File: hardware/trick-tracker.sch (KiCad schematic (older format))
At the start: 52 parts, among them IC1 BMX160, J1 USB4105-GF-A, J2 S2B-PH-K, J3 QWiiC, J4 MEM2061-01-188-00-A, J6 QWiiC, P1 SMTB-1240-S-R, U1 MS88SF2, U2 DPS368XTSA1, U4 MCP73831/OT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

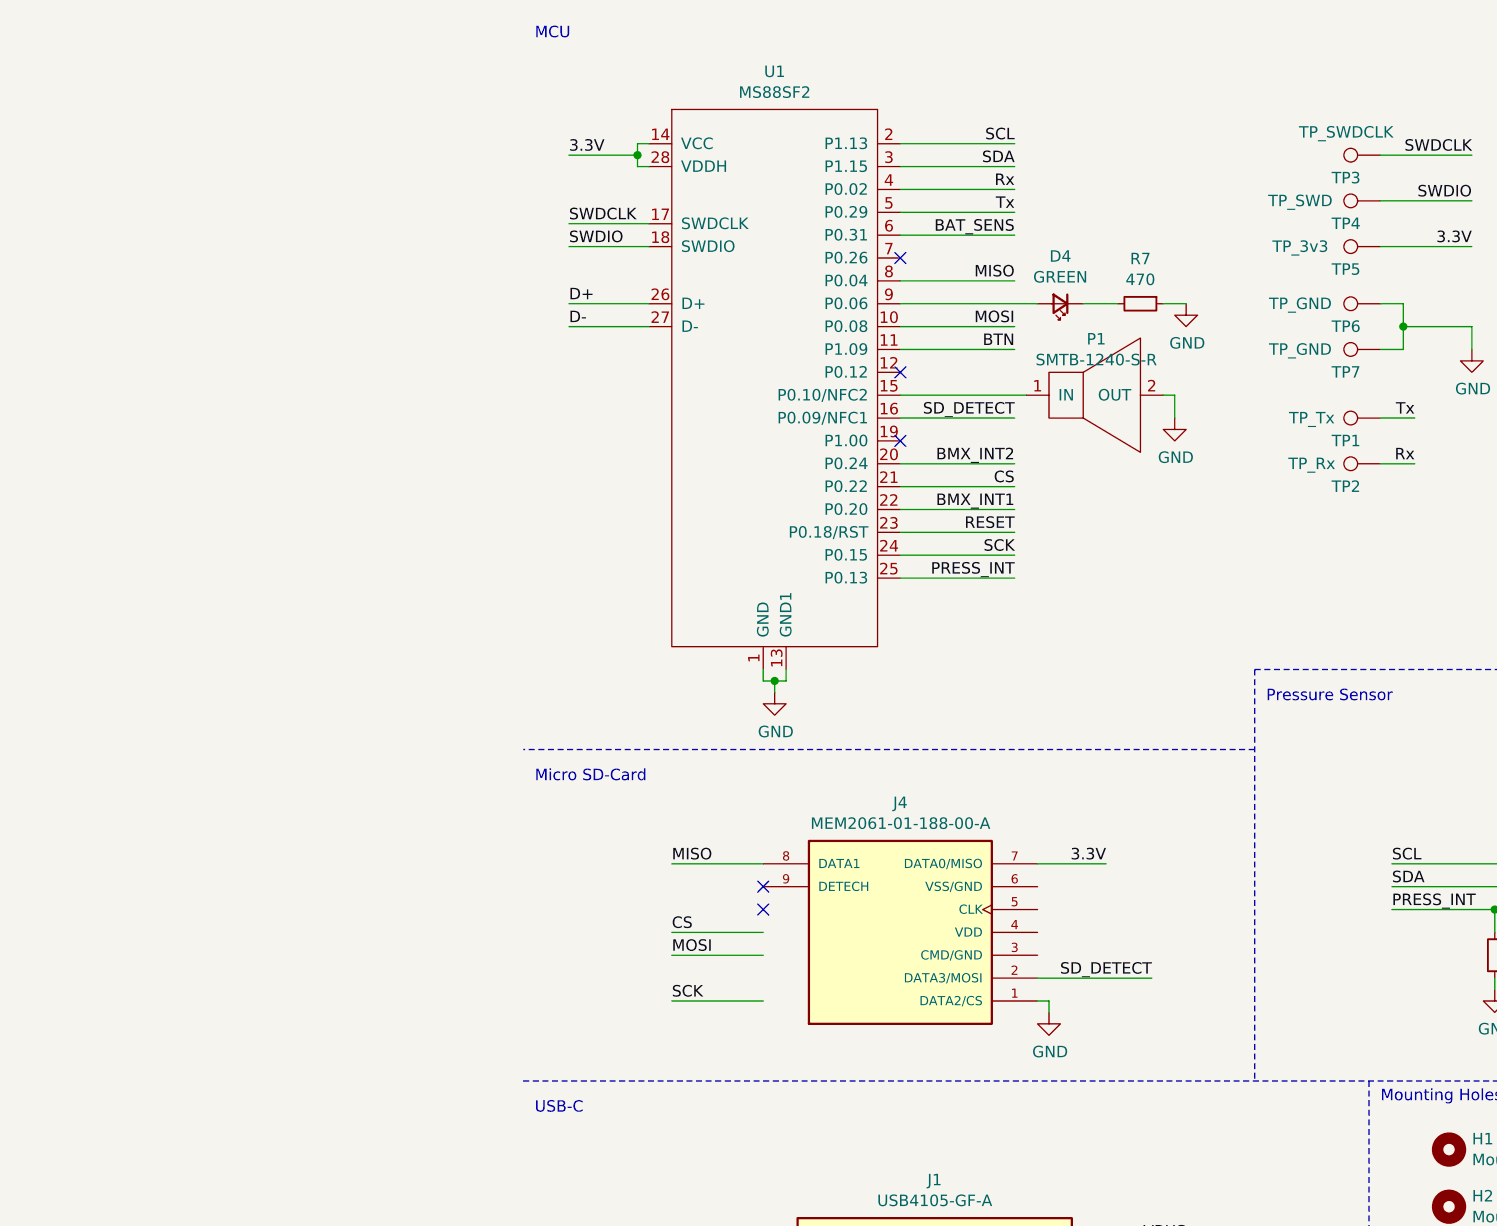
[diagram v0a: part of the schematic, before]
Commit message: Changed Layout to use ESP32 instead of nRF52
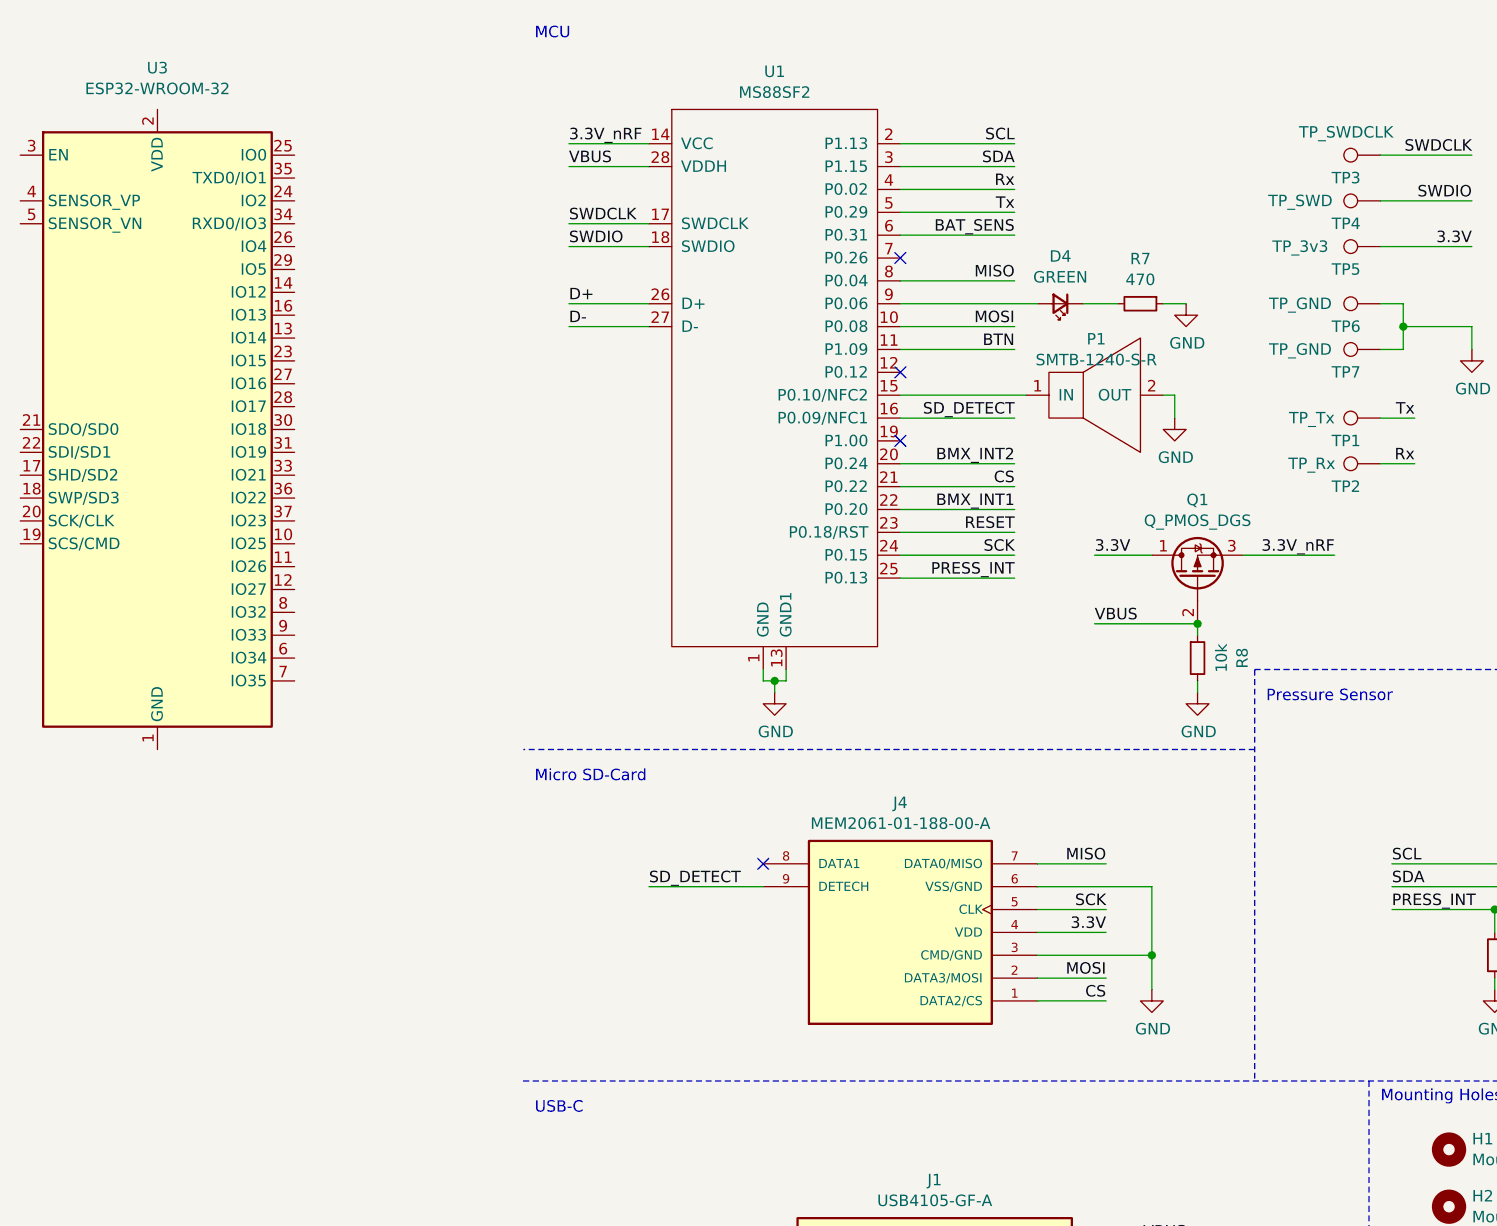
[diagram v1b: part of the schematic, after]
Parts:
- added Q1: Q_PMOS_DGS, symbol Device:Q_PMOS_DGS
- added R8: 10k, Resistor_SMD:R_0603_1608Metric, symbol Device:R_Small
- added U3: ESP32-WROOM-32, RF_Module:ESP32-WROOM-32, symbol RF_Module:ESP32-WROOM-32
- J4: footprint MEM2061-01-188-00-A_REVA:GCT_MEM2061-01-188-00-A_REVA -> GCT_MEM2051-00-195-00-A; MANUFACTURER (none) -> GCT
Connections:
- net 3.3V: now also J4.4 (VDD), Q1.1 (D); no longer J4.7 (DATA0/MISO), U1.14 (VCC), U1.28 (VDDH)
- net CS: now also J4.1 (DATA2/CS)
- net GND: now also J4.3 (CMD/GND), J4.6 (VSS/GND), R8.2; no longer J4.1 (DATA2/CS)
- net MISO: now also J4.7 (DATA0/MISO); no longer J4.8 (DATA1)
- net MOSI: now also J4.2 (DATA3/MOSI)
- net SCK: now also J4.5 (CLK)
- net SD_DETECT: now also J4.9 (DETECH); no longer J4.2 (DATA3/MOSI)
- net VBUS: now also U1.28 (VDDH), Q1.2 (G), R8.1
- new net: U3.1 (GND), U3.15 (GND), U3.38 (GND), U3.39 (GND)
- new net 3.3V_nRF: Q1.3 (S), U1.14 (VCC)
- no-connect marks 12 -> 11
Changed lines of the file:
@@
 Wire Wire Line
 	1600 3400 1550 3400
-Text Label 700  1100 0    50   ~ 0
-3.3V
-Wire Wire Line
-	1050 1150 1000 1150
-Wire Wire Line
-	1050 1050 1000 1050
-Wire Wire Line
-	1000 1050 1000 1100
-Wire Wire Line
-	700  1100 1000 1100
-Connection ~ 1000 1100
-Wire Wire Line
-	1000 1100 1000 1150
 $Comp
 L Device:D_Schottky D1
@@
 F 0 "J4" H 2150 5067 50  0000 C CNN
 F 1 "MEM2061-01-188-00-A" H 2150 4976 50  0000 C CNN
-F 2 "MEM2061-01-188-00-A_REVA:GCT_MEM2061-01-188-00-A_REVA" H 2150 4500 50  0001 L BNN
+F 2 "GCT_MEM2051-00-195-00-A" H 2150 4500 50  0001 L BNN
 F 3 "" H 2150 4500 50  0001 L BNN
+F 4 "GCT" H 2150 4500 50  0001 C CNN "MANUFACTURER"
 	1    2150 4500
 	1    0    0    -1
@@
 	1    0    0    -1
 $EndComp
+Text Label 3050 4500 2    50   ~ 0
+3.3V
 Text Label 3050 4200 2    50   ~ 0
-3.3V
-Wire Wire Line
-	3050 4200 2750 4200
-Text Label 1150 4200 0    50   ~ 0
 MISO
-Text Label 1150 4600 0    50   ~ 0
+Text Label 3050 4700 2    50   ~ 0
 MOSI
-Text Label 1150 4800 0    50   ~ 0
+Text Label 3050 4400 2    50   ~ 0
 SCK
-NoConn ~ 1550 4300
-NoConn ~ 1550 4400
-Text Label 1150 4500 0    50   ~ 0
+Text Label 3050 4800 2    50   ~ 0
 CS
 $Comp
 L power:GND #PWR0130
 U 1 1 60AF2CE9
-P 2800 4850
-F 0 "#PWR0130" H 2800 4600 50  0001 C CNN
-F 1 "GND" H 2805 4677 50  0000 C CNN
-F 2 "" H 2800 4850 50  0001 C CNN
-F 3 "" H 2800 4850 50  0001 C CNN
-	1    2800 4850
-	1    0    0    -1
-$EndComp
-Wire Wire Line
-	2800 4850 2800 4800
-Wire Wire Line
-	2800 4800 2750 4800
-Wire Wire Line
-	1550 4800 1150 4800
-Wire Wire Line
-	1150 4600 1550 4600
-Wire Wire Line
-	1550 4500 1150 4500
-Wire Wire Line
-	1150 4200 1550 4200
+P 3250 4750
+F 0 "#PWR0130" H 3250 4500 50  0001 C CNN
+F 1 "GND" H 3255 4577 50  0000 C CNN
+F 2 "" H 3250 4750 50  0001 C CNN
+F 3 "" H 3250 4750 50  0001 C CNN
+	1    3250 4750
+	1    0    0    -1
+$EndComp
 $Comp
 L Device:R_Small R7
@@
 Wire Wire Line
 	2650 2850 2150 2850
-Text Label 3250 4700 2    50   ~ 0
+Text Label 1050 4300 0    50   ~ 0
 SD_DETECT
-Wire Wire Line
-	3250 4700 2750 4700
 Text Label 2650 2250 2    50   ~ 0
 SD_DETECT
@@
 Wire Wire Line
 	4350 1850 4350 1950
+Wire Wire Line
+	700  1050 1050 1050
+$Comp
+L Device:Q_PMOS_DGS Q1
+U 1 1 6166D587
+P 3450 2950
+F 0 "Q1" V 3792 2950 50  0000 C CNN
+F 1 "Q_PMOS_DGS" V 3701 2950 50  0000 C CNN
+F 2 "" H 3650 3050 50  0001 C CNN
+F 3 "~" H 3450 2950 50  0001 C CNN
+	1    3450 2950
+	0    -1   -1   0
+$EndComp
+Text Label 3000 2850 0    50   ~ 0
+3.3V
+Wire Wire Line
+	3000 2850 3250 2850
+Text Label 4050 2850 2    50   ~ 0
+3.3V_nRF
+Wire Wire Line
+	4050 2850 3650 2850
+Text Label 3000 3150 0    50   ~ 0
+VBUS
+Text Label 700  1150 0    50   ~ 0
+VBUS
+Wire Wire Line
+	1050 1150 700  1150
+Wire Wire Line
+	3000 3150 3450 3150
+$Comp
+L Device:R_Small R8
+U 1 1 616A1F0D
+P 3450 3300
+F 0 "R8" V 3646 3300 50  0000 C CNN
+F 1 "10k" V 3555 3300 50  0000 C CNN
+F 2 "Resistor_SMD:R_0603_1608Metric" H 3450 3300 50  0001 C CNN
+F 3 "~" H 3450 3300 50  0001 C CNN
+	1    3450 3300
+	1    0    0    -1
+$EndComp
+$Comp
+L power:GND #PWR0121
+U 1 1 616A2F85
+P 3450 3450
+F 0 "#PWR0121" H 3450 3200 50  0001 C CNN
+F 1 "GND" H 3455 3277 50  0000 C CNN
+F 2 "" H 3450 3450 50  0001 C CNN
+F 3 "" H 3450 3450 50  0001 C CNN
+	1    3450 3450
+	1    0    0    -1
+$EndComp
+Wire Wire Line
+	3450 3150 3450 3200
+Connection ~ 3450 3150
+Wire Wire Line
+	3450 3400 3450 3450
+Text Label 700  1050 0    50   ~ 0
+3.3V_nRF
+$Comp
+L RF_Module:ESP32-WROOM-32 U3
+U 1 1 61E158C8
+P -1100 2300
+F 0 "U3" H -1100 3881 50  0000 C CNN
+F 1 "ESP32-WROOM-32" H -1100 3790 50  0000 C CNN
+F 2 "RF_Module:ESP32-WROOM-32" H -1100 800 50  0001 C CNN
+F 3 "https://www.espressif.com/sites/default/files/documentation/esp32-wroom-32_datasheet_en.pdf" H -1400 2350 50  0001 C CNN
+	1    -1100 2300
+	1    0    0    -1
+$EndComp
+Wire Wire Line
+	3050 4800 2750 4800
+Wire Wire Line
+	3050 4700 2750 4700
+Wire Wire Line
+	3050 4500 2750 4500
+Wire Wire Line
+	2750 4400 3050 4400
+Wire Wire Line
+	3050 4200 2750 4200
+Wire Wire Line
+	2750 4300 3250 4300
+Wire Wire Line
+	3250 4300 3250 4600
+Wire Wire Line
+	2750 4600 3250 4600
+Connection ~ 3250 4600
+Wire Wire Line
+	3250 4600 3250 4750
+NoConn ~ 1550 4200
+Wire Wire Line
+	1550 4300 1050 4300
 $EndSCHEMATC
